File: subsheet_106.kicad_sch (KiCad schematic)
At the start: 44 parts, among them P01 1K, T04 BC557B, T05 BC337-40, T06 BC547B, T07 BC547B, T08 BC557B, T09 BC547B, T10 BC547B

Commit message: update comments in cartridge
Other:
- title: Conversion du Thomson MO5 — Unité centrale v1 -> Conversion du Thomson MO5 — Unité centrale v2
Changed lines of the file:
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@@
   (paper "A4" portrait)
   (title_block
-    (title "Conversion du Thomson MO5 — Unité centrale v1")
-    (date "2024-12-30")
-    (rev "v1.0.0-rc2")
+    (title "Conversion du Thomson MO5 — Unité centrale v2")
+    (date "2025-02-08")
+    (rev "v2.0.0-alpha")
     (comment 1 "http://github.com/sporniket/kicad-conversions--thomson-mo5--v1")
-    (comment 3 "Gate Array Motorola MCA 1300 ALS")
-    (comment 4 "Reference : POP5001 501994-01")
+    (comment 3 "Gate Array EFCIS")
   )
   (junction (at 177.8 130.81) (diameter 0) (color 0 0 0 0)

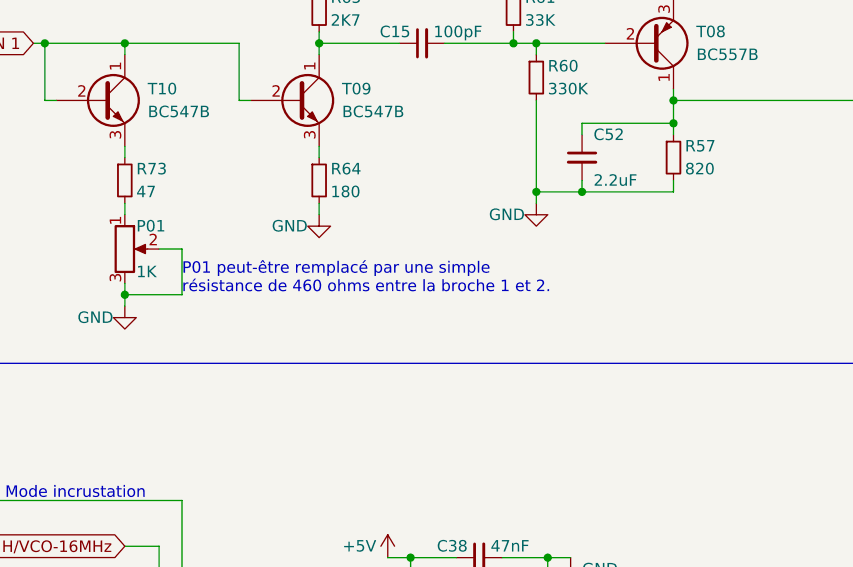
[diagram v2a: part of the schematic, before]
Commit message: fixed some naming, assigned footprints to symbols without one, added them to pcb
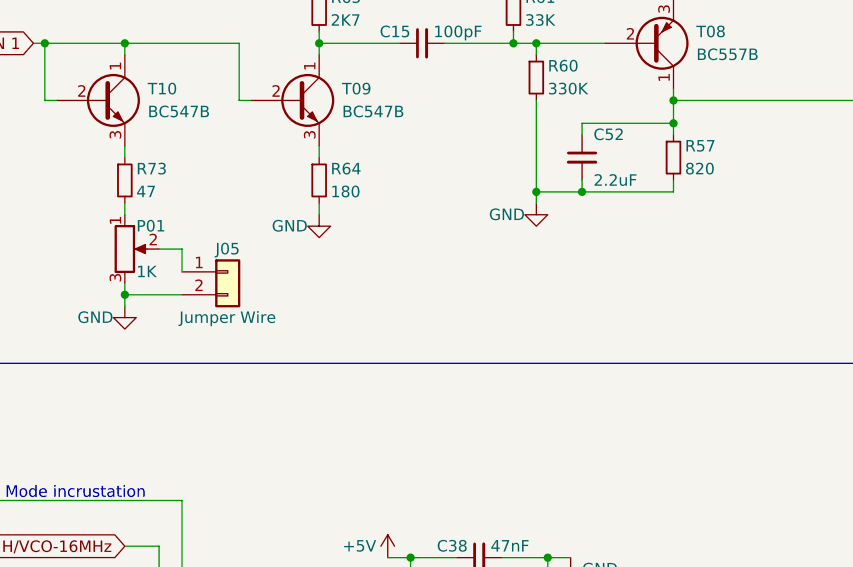
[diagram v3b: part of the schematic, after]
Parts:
- added J05: Jumper Wire, thomson-moto-passives:Passive_THT_jumper_wire_W2.54mm_L12.70mm, symbol Connector_Generic:Conn_01x02
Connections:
- net GND: now also J05.2 (Pin_2); no longer P01.2
- new net: J05.1 (Pin_1), P01.2
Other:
- note removed: "P01 peut-être remplacé par une simple résistance de 460 ohms entre la broche 1 et 2."
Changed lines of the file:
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@@
-    (stroke (width 0) (type default))
-  )
-  (wire (pts (xy 46.99 88.9) (xy 46.99 83.82))
     (stroke (width 0) (type default))
   )
@@
   )
   (wire (pts (xy 62.23 62.23) (xy 62.23 60.96))
+    (stroke (width 0) (type default))
+  )
+  (wire (pts (xy 46.99 86.36) (xy 46.99 83.82))
     (stroke (width 0) (type default))
   )
@@
   )
   (text "Vers I48" (at 189.23 36.83 0)
-    (effects (font (size 1.27 1.27)) (justify left bottom))
-  )
-  (text "P01 peut-être remplacé par une simple \nrésistance de 460 ohms entre la broche 1 et 2."
-    (at 46.99 88.9 0)
     (effects (font (size 1.27 1.27)) (justify left bottom))
   )
@@
         )
       )
+    )
+  )
+  (symbol (lib_id "Connector_Generic:Conn_01x02") (at 52.07 86.36 0) (unit 1)
+    (in_bom yes) (on_board yes) (dnp no)
+    (property "Reference" "J05" (at 52.07 83.82 0)
+      (effects (font (size 1.27 1.27)))
+    )
+    (property "Value" "Jumper Wire" (at 52.07 91.44 0)
+      (effects (font (size 1.27 1.27)))
+    )
+    (property "Footprint" "thomson-moto-passives:Passive_THT_jumper_wire_W2.54mm_L12.70mm" (at 52.07 86.36 0)
+      (effects (font (size 1.27 1.27)) hide)
+    )
+    (property "Datasheet" "~" (at 52.07 86.36 0)
+      (effects (font (size 1.27 1.27)) hide)
+    )
+    (pin "2")
+    (pin "1")
+    (instances
+      (project "UC-50-001"
+        (path "/e63e39d7-6ac0-4ffd-8aa3-1841a4541b55/706ec47c-3d4a-4bde-bb8b-c4f8dcc96c45"
+          (reference "J05") (unit 1)
+        )
+      )

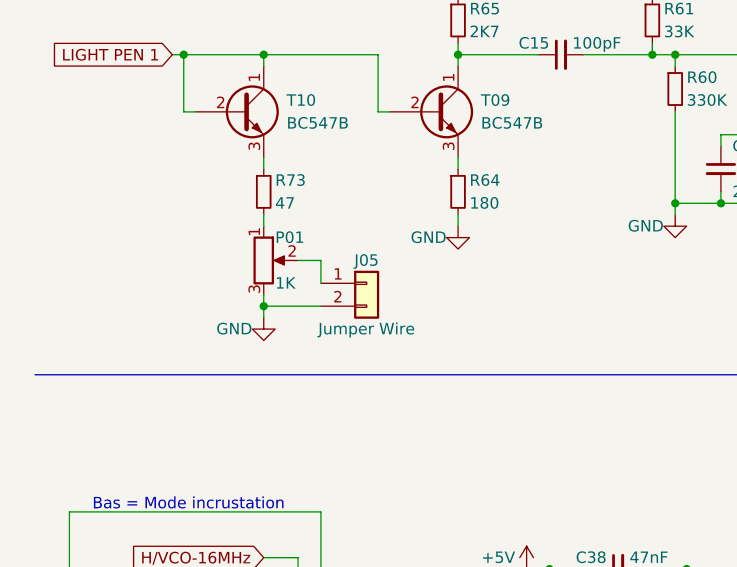
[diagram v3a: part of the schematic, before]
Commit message: pcb : moved components, south-east corner, fixed links between P01 and J05
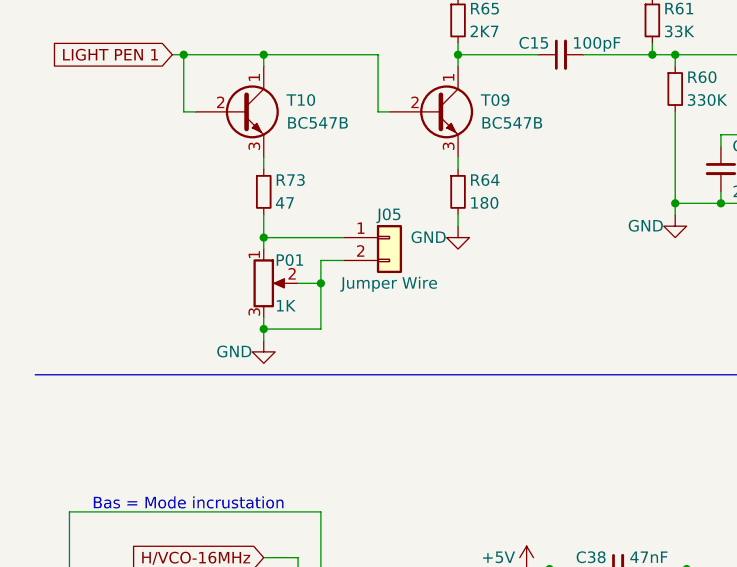
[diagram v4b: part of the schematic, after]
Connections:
- net GND: now also P01.2
- net at P01.1, R73.2: now also J05.1 (Pin_1)
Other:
- moved on the sheet: J05, P01

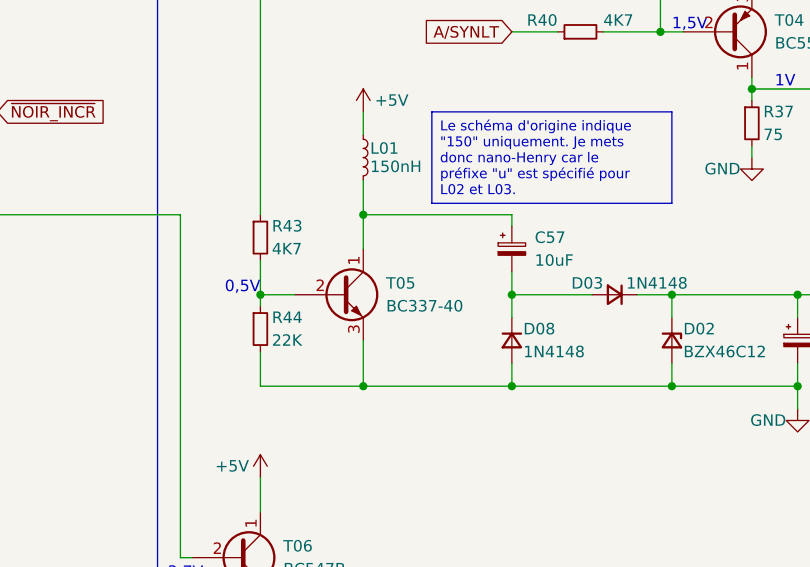
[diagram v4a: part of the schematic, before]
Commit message: pcb : moved component, middle north-east corner
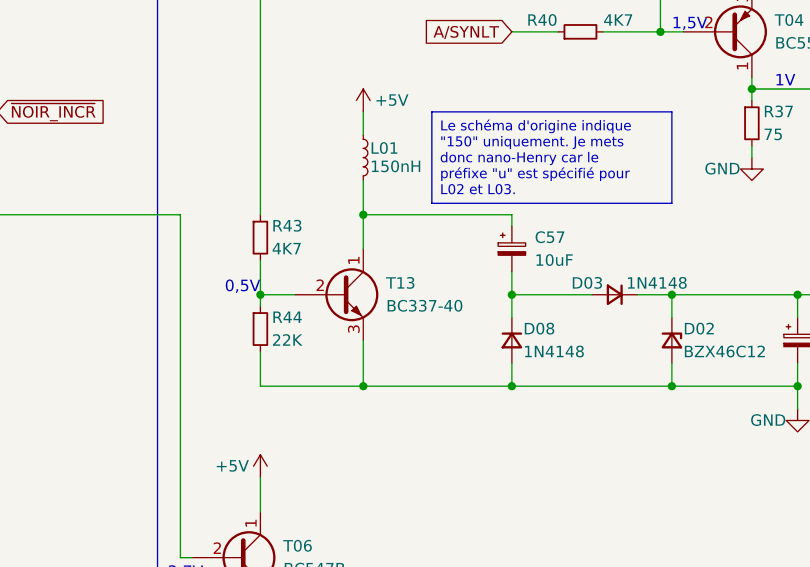
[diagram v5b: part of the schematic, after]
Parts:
- renumbered T05 to T13
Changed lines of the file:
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@@
   (symbol (lib_id "Device:Q_NPN_CBE") (at 132.08 173.99 0) (unit 1)
     (in_bom yes) (on_board yes) (dnp no)
-    (property "Reference" "T05" (at 137.16 172.72 0)
+    (property "Reference" "T13" (at 137.16 172.72 0)
       (effects (font (size 1.27 1.27)) (justify left))
     )
@@
       (project "UC-50-001"
         (path "/e63e39d7-6ac0-4ffd-8aa3-1841a4541b55/706ec47c-3d4a-4bde-bb8b-c4f8dcc96c45"
-          (reference "T05") (unit 1)
+          (reference "T13") (unit 1)
         )
       )

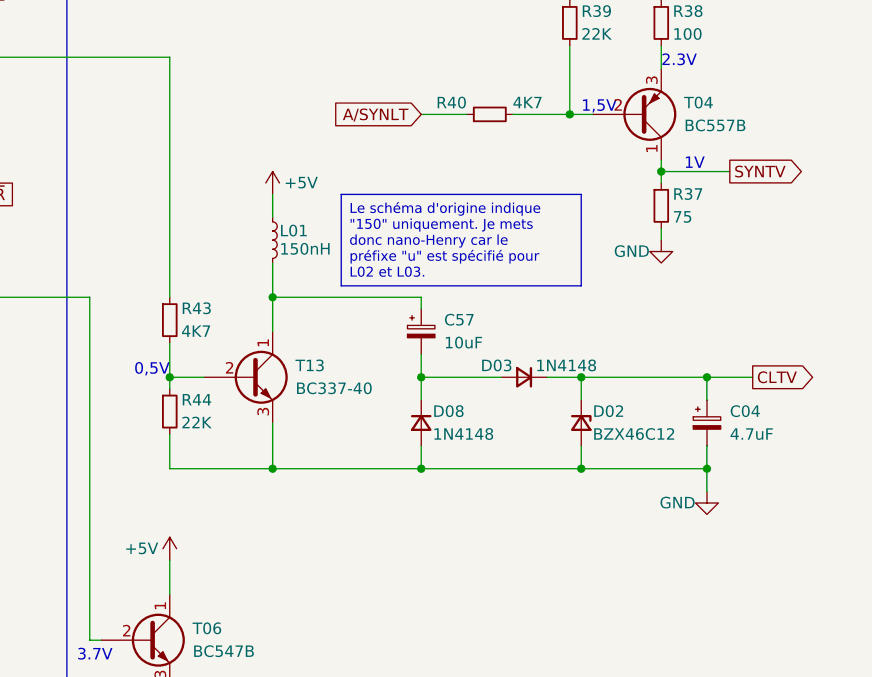
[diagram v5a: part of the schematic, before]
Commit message: pcb : done, fixed CLTV circuitry
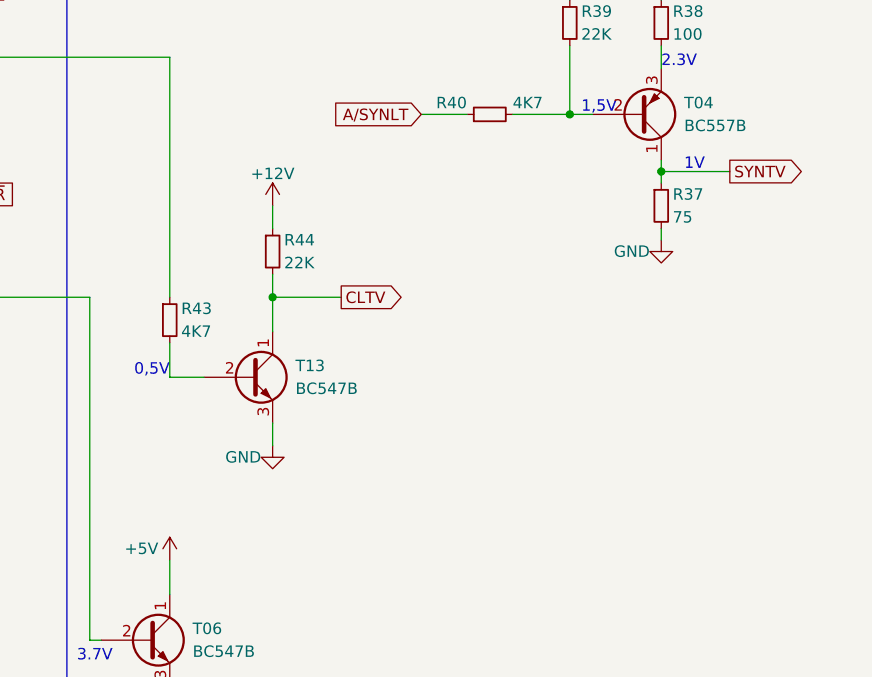
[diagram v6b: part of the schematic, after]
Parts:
- removed C04: 4.7uF, commons-passives_THT:Passive_THT_capacitor_polarized_EU_W2.54mm_L5.08mm, symbol Device:C_Polarized_Small
- removed C57: 10uF, commons-passives_THT:Passive_THT_capacitor_polarized_EU_W2.54mm_L5.08mm, symbol Device:C_Polarized_Small
- removed D02: BZX46C12, commons-passives_THT:Passive_THT_diode_W2.54mm_L12.70mm, symbol Device:D_Zener_Small
- removed D03, D08: 1N4148, commons-passives_THT:Passive_THT_diode_W2.54mm_L12.70mm, symbol Device:D_Small
- removed L01: 150nH, commons-passives_THT:Passive_THT_inductor_W5.08mm_L12.70mm, symbol Device:L_Small
- T13: value BC337-40 -> BC547B
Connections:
- net CLTV: now also R44.2, T13.1 (C)
- net GND: no longer R44.2
- net at R43.2, T13.2 (B): no longer R44.1
- new net +12V: R44.1
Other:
- moved on the sheet: R44

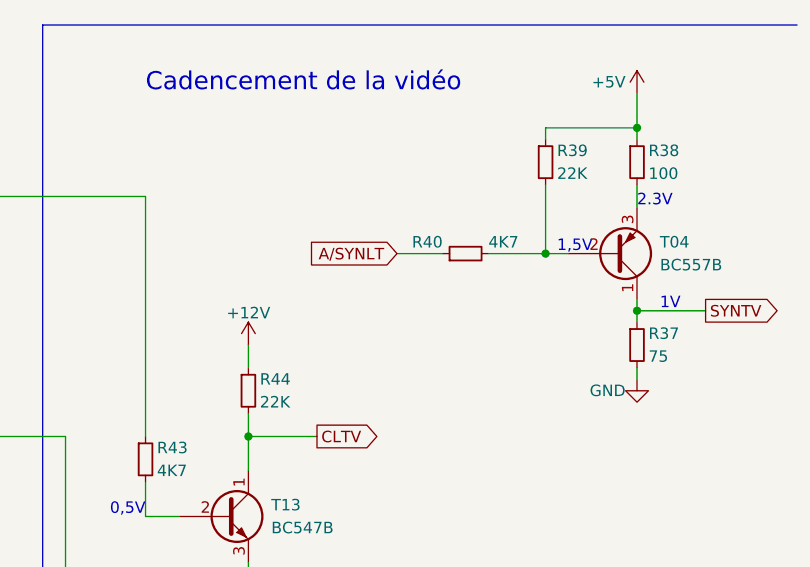
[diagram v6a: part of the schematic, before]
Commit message: Done #20 : missing capacitors C65, C69, C70, C80 (footprints on PCB, not found on schematics)
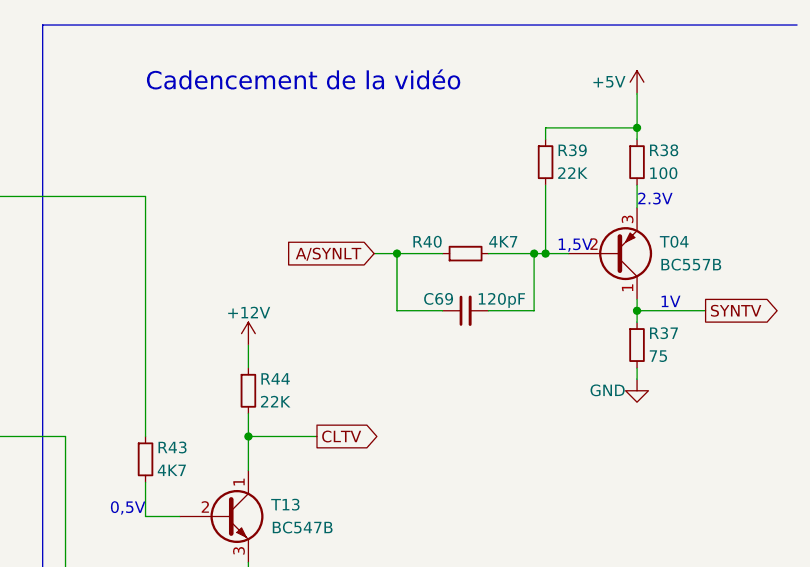
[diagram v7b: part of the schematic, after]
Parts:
- added C69: 120pF, commons-passives_THT:Passive_THT_capacitor_mlcc_W2.54mm_L5.08mm, symbol Device:C_Small
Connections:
- net A/SYNLT: now also C69.1
- net at R39.2, R40.2, T04.2 (B): now also C69.2

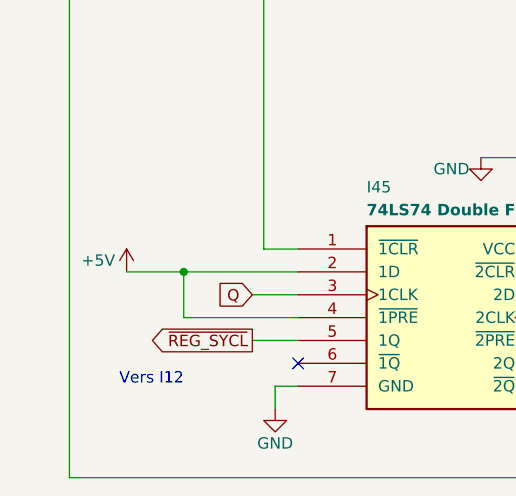
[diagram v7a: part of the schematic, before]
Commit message: fixed I45 : pin 2 and 4 are now grounded
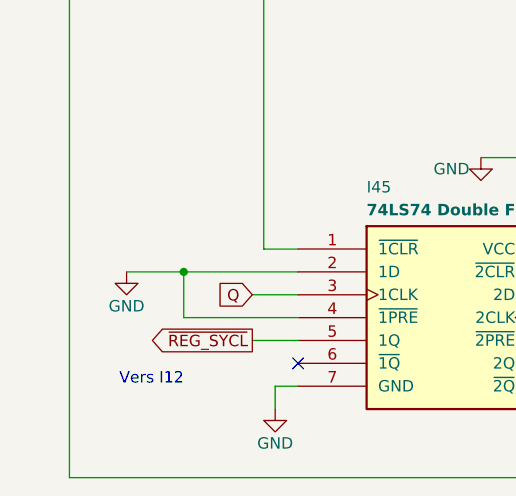
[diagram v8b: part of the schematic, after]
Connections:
- net +5V: no longer I45.2 (1D), I45.4 (~{1PRE})
- net GND: now also I45.2 (1D), I45.4 (~{1PRE})
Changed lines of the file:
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@@
+    )
+  )
+  (symbol (lib_id "power:GND") (at 25.4 205.74 0) (unit 1)
+    (in_bom yes) (on_board yes) (dnp no)
+    (property "Reference" "#PWR035" (at 25.4 212.09 0)
+      (effects (font (size 1.27 1.27)) hide)
+    )
+    (property "Value" "GND" (at 25.4 209.55 0)
+      (effects (font (size 1.27 1.27)))
+    )
+    (property "Footprint" "" (at 25.4 205.74 0)
+      (effects (font (size 1.27 1.27)) hide)
+    )
+    (property "Datasheet" "" (at 25.4 205.74 0)
+      (effects (font (size 1.27 1.27)) hide)
+    )
+    (pin "1")
+    (instances
+      (project "UC-50-001"
+        (path "/e63e39d7-6ac0-4ffd-8aa3-1841a4541b55/706ec47c-3d4a-4bde-bb8b-c4f8dcc96c45"
+          (reference "#PWR035") (unit 1)
+        )
+      )
     )
   )
@@
         )
       )
-    )
-  )
-  (symbol (lib_id "power:+5V") (at 25.4 205.74 0) (unit 1)
-    (in_bom yes) (on_board yes) (dnp no)
-    (property "Reference" "#PWR0271" (at 25.4 209.55 0)
-      (effects (font (size 1.27 1.27)) hide)
-    )
-    (property "Value" "+5V" (at 24.13 204.47 0)
-      (effects (font (size 1.27 1.27)) (justify right))
-    )
-    (property "Footprint" "" (at 25.4 205.74 0)
-      (effects (font (size 1.27 1.27)) hide)
-    )
-    (property "Datasheet" "" (at 25.4 205.74 0)
-      (effects (font (size 1.27 1.27)) hide)
-    )
-    (pin "1")
-    (instances
-      (project "UC-50-001"
-        (path "/e63e39d7-6ac0-4ffd-8aa3-1841a4541b55/706ec47c-3d4a-4bde-bb8b-c4f8dcc96c45"
-          (reference "#PWR0271") (unit 1)
-        )
-      )
